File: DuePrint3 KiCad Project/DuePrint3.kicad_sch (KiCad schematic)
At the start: 49 parts, among them J1 430452412, J10 436500215, J11 M20-9990245, J12 M20-9990245, J13 EHT-125-01-S-D, J14 EHT-110-01-S-D, J15 EHT-125-01-S-D, J2 PPPC161LFBN-RC, J3 PPPC161LFBN-RC, J4 6P2C, J5 6P2C, J6 M20-9990345, J7 436500215, J8 436500815, J9 430451812, U1 SN74AHCT125DR

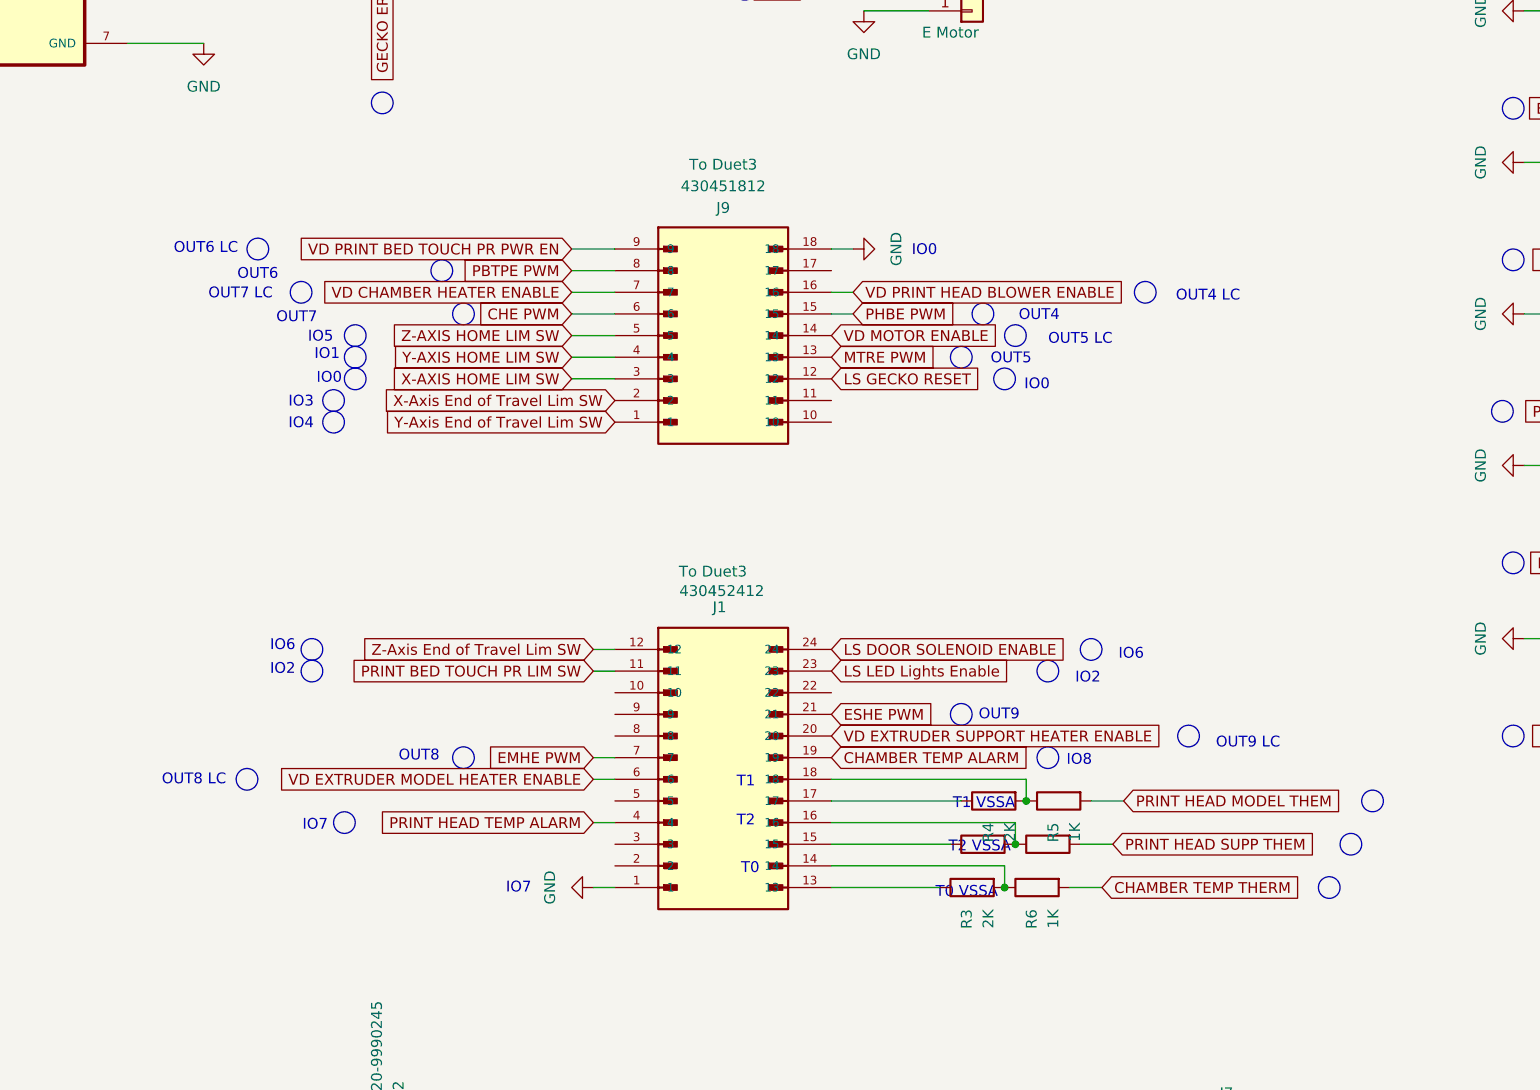
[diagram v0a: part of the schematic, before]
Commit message: Reformat Duet3 connectors
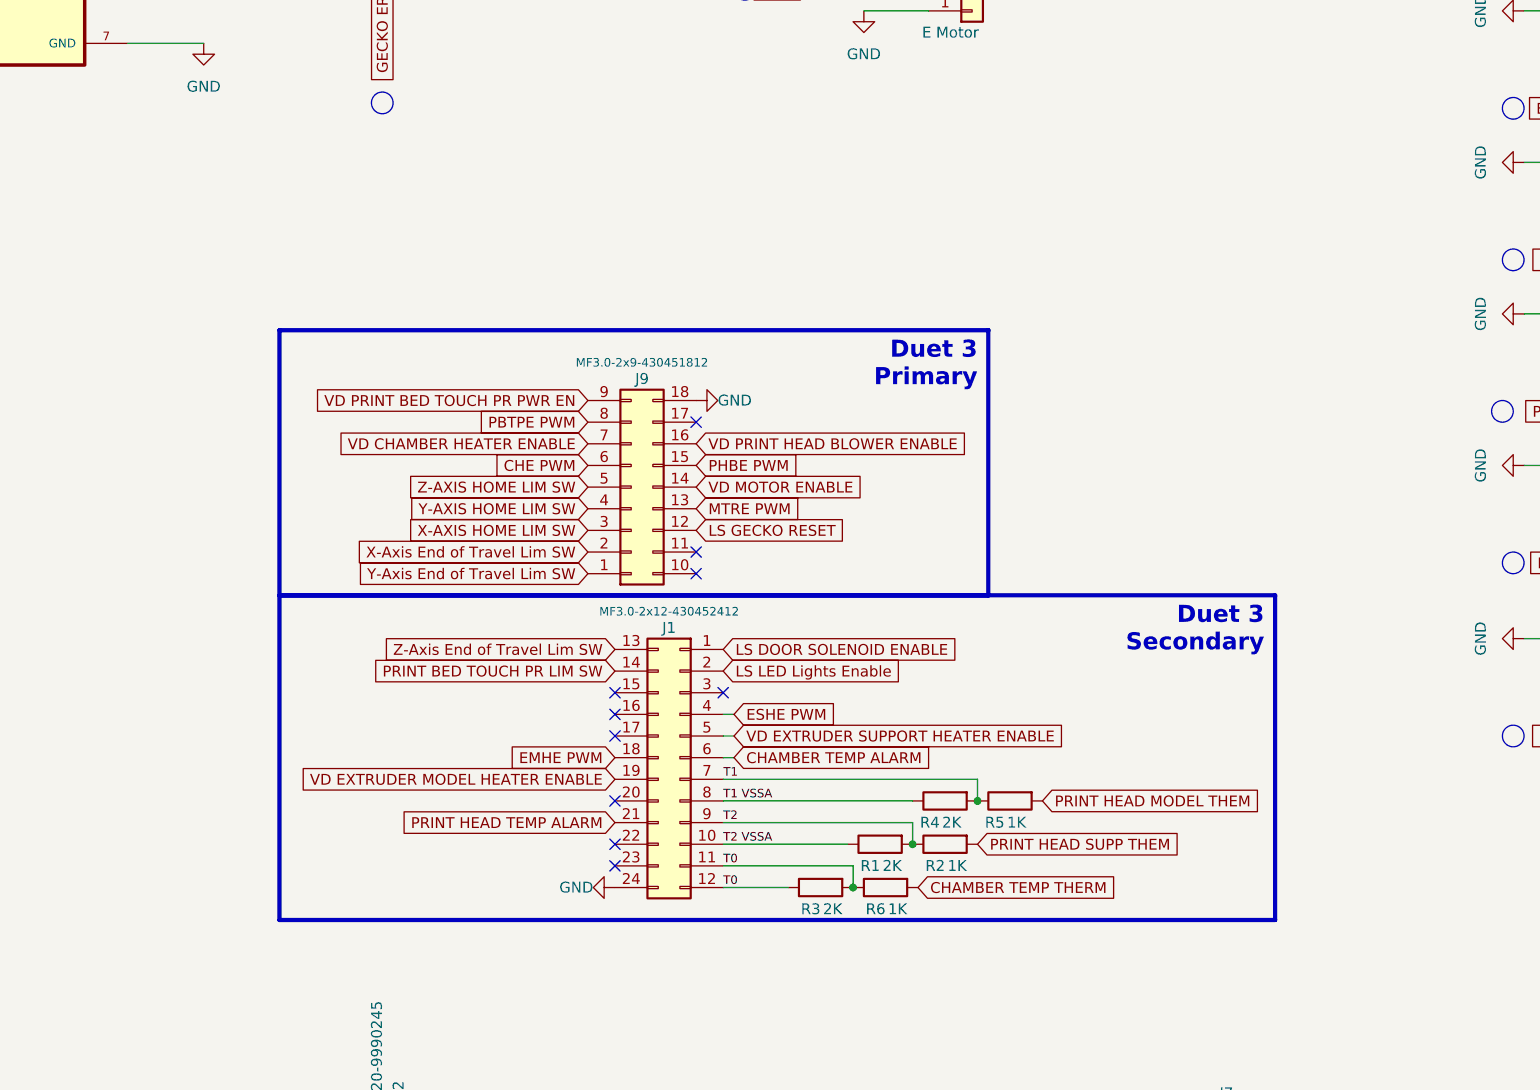
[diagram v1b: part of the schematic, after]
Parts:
- removed J1: 430452412, Connector_Molex:Molex_Micro-Fit_3.0_43045-2412_2x12_P3.00mm_Vertical, symbol 430452427:430452427
- removed J9: 430451812, Connector_Molex:Molex_Micro-Fit_3.0_43045-1812_2x09_P3.00mm_Vertical, symbol Project:430451827
- added J1: MF3.0-2x12-430452412, Connector_Molex:Molex_Micro-Fit_3.0_43045-2412_2x12_P3.00mm_Vertical, symbol Connector_Generic:Conn_02x12_Top_Bottom
- added J9: MF3.0-2x9-430451812, Connector_Molex:Molex_Micro-Fit_3.0_43045-1812_2x09_P3.00mm_Vertical, symbol Connector_Generic:Conn_02x09_Top_Bottom
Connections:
- net CHAMBER HEATER ENABLE: now also J9.6 (Pin_6)
- net CHAMBER TEMP ALARM: now also J1.6 (Pin_6)
- net EMHE PWM: now also J1.18 (Pin_18)
- net ESHE PWM: now also J1.4 (Pin_4)
- net GND: now also J1.24 (Pin_24), J9.18 (Pin_18)
- net LS DOOR SOLENOID ENABLE: now also J1.1 (Pin_1)
- net LS GECKO RESET: now also J9.12 (Pin_12)
- net LS LED Lights Enable: now also J1.2 (Pin_2)
- net MOTOR ENABLE: now also J9.13 (Pin_13)
- net PBTPE PWM: now also J9.8 (Pin_8)
- net PHBE PWM: now also J9.15 (Pin_15)
- net PRINT BED TOUCH PR LIM SW: now also J1.14 (Pin_14)
- net PRINT HEAD TEMP ALARM: now also J1.21 (Pin_21)
- net VD CHAMBER HEATER ENABLE: now also J9.7 (Pin_7)
- net VD EXTRUDER MODEL HEATER ENABLE: now also J1.19 (Pin_19)
- net VD EXTRUDER SUPPORT HEATER ENABLE: now also J1.5 (Pin_5)
- net VD MOTOR ENABLE: now also J9.14 (Pin_14)
- net VD PRINT BED TOUCH PR PWR EN: now also J9.9 (Pin_9)
- net VD PRINT HEAD BLOWER ENABLE: now also J9.16 (Pin_16)
- net X-AXIS HOME LIM SW: now also J9.3 (Pin_3)
- net X-Axis End of Travel Lim SW: now also J9.2 (Pin_2)
- net Y-AXIS HOME LIM SW: now also J9.4 (Pin_4)
- net Y-Axis End of Travel Lim SW: now also J9.1 (Pin_1)
- net Z-AXIS HOME LIM SW: now also J9.5 (Pin_5)
- net Z-Axis End of Travel Lim SW: now also J1.13 (Pin_13)
- net T1 VSSA: now reaches R4.1
- net T1 VSSA: now also J1.8 (Pin_8)
- net T1: now reaches R4.2, R5.1
- net T1: now also J1.7 (Pin_7)
- net T0: now reaches R3.1
- net T0: now also R3.2, R6.1, J1.11 (Pin_11), J1.12 (Pin_12)
- net T2: now reaches R1.2, R2.1
- net T2: now also J1.9 (Pin_9)
- net T2 VSSA: now reaches R1.1
- net T2 VSSA: now also J1.10 (Pin_10)
- no-connect marks 0 -> 10
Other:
- note added: "Duet 3 Primary"
- note added: "Duet 3 Secondary"
- note removed: "IO0"
- note removed: "IO1"
- note removed: "IO2"
- note removed: "IO3"
- note removed: "IO4"
- note removed: "IO5"
- note removed: "IO6"
- note removed: "IO7"
- note removed: "IO8"
- note removed: "OUT4"
- note removed: "OUT4 LC"
- note removed: "OUT5"
- note removed: "OUT5 LC"
- note removed: "OUT6"
- note removed: "OUT6 LC"
- note removed: "OUT7"
- note removed: "OUT7 LC"
- note removed: "OUT8"
- note removed: "OUT8 LC"
- note removed: "OUT9"
- note removed: "OUT9 LC"
- note removed: "T0"
- note removed: "T0 VSSA"
- note removed: "T1"
- note removed: "T1 VSSA"
- note removed: "T2"
- note removed: "T2 VSSA"
- moved on the sheet: R3, R4, R5, R6

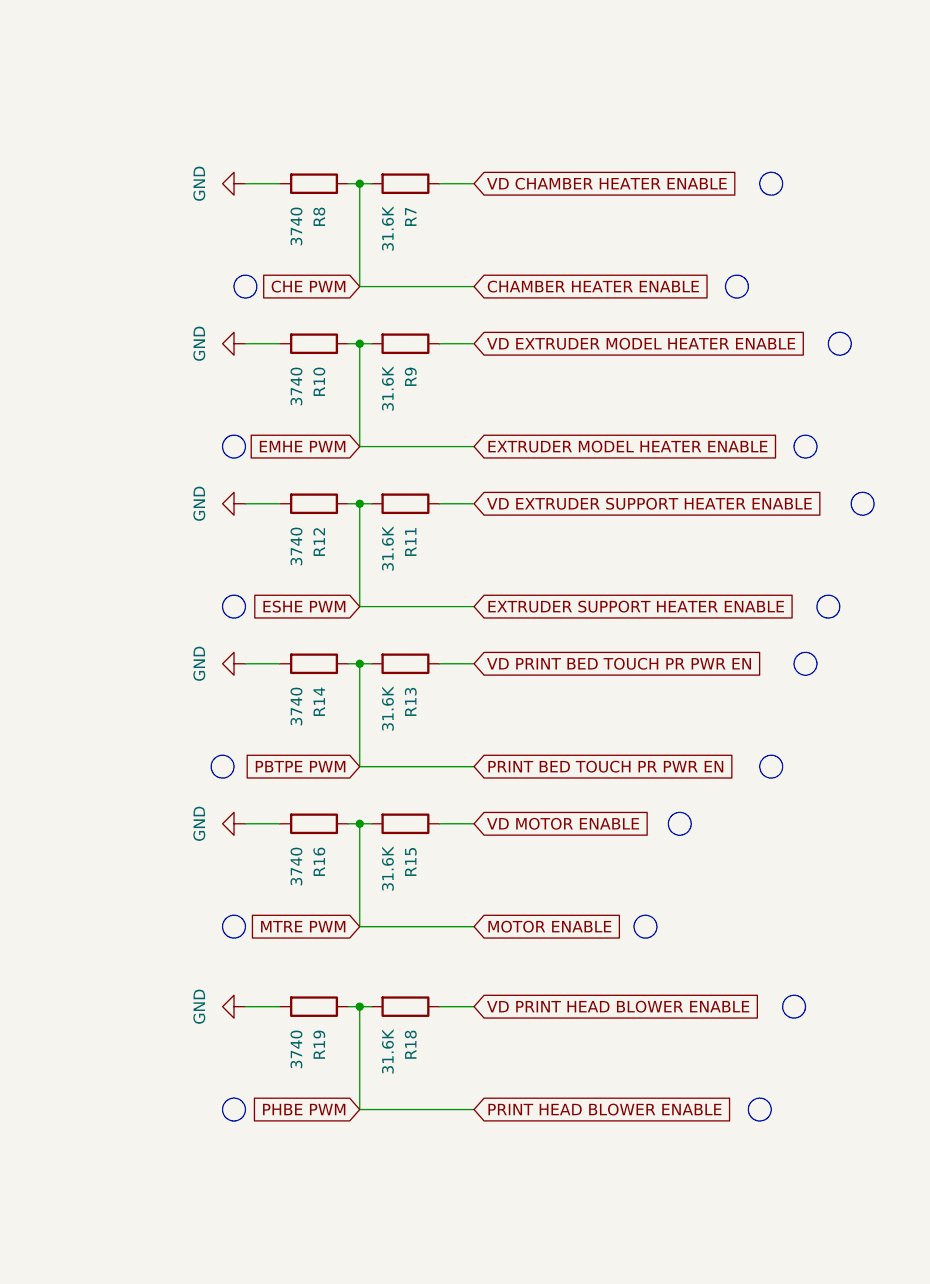
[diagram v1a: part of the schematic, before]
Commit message: Voltage Dividers
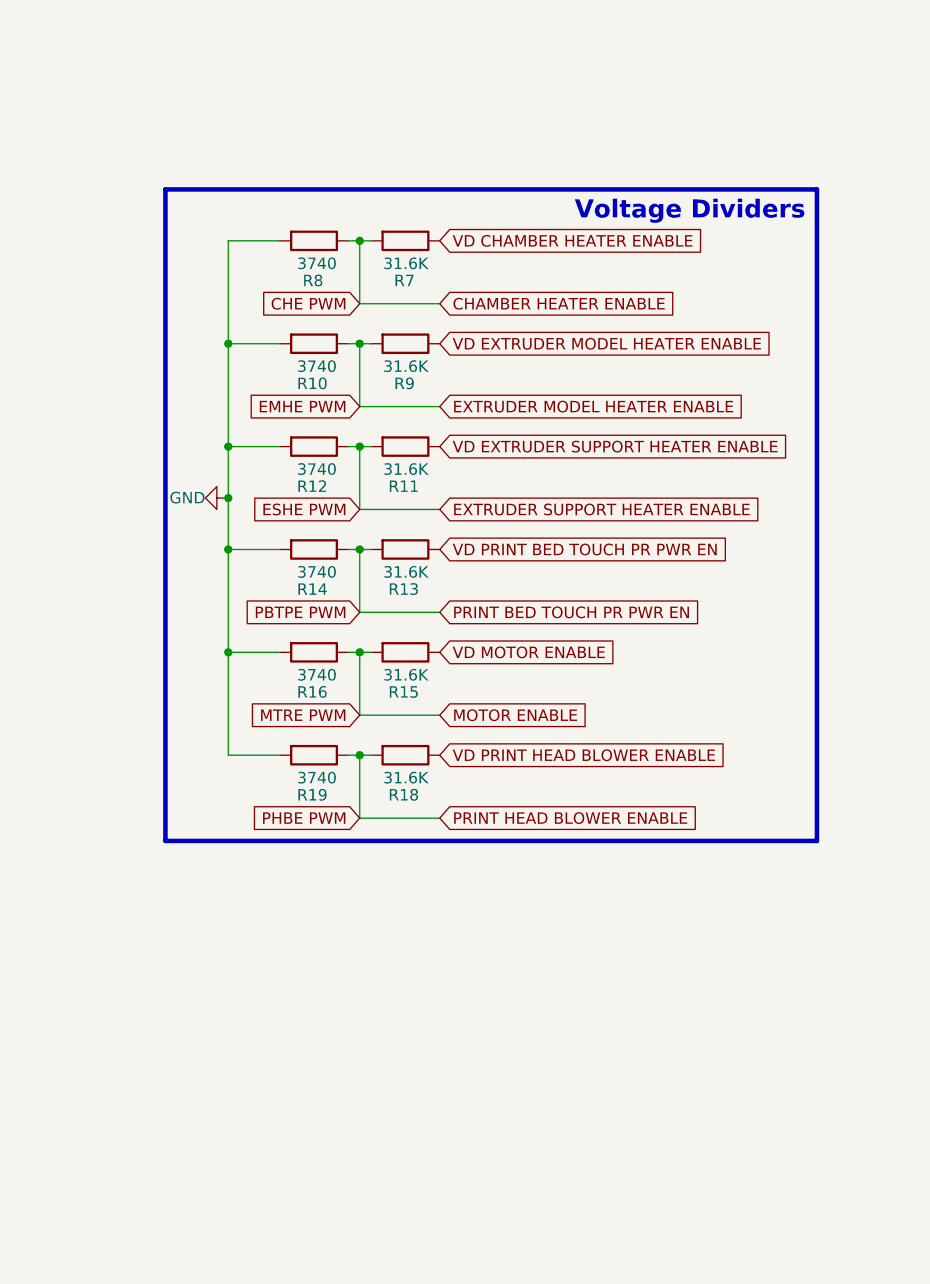
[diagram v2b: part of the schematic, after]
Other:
- note added: "Voltage Dividers"
- moved on the sheet: R11, R12, R13, R14, R15, R16, R18, R19, R7, R8

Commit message: Level shifter
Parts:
- D1: value 100v 1a -> 100v 1A
- J8: value 436500815 -> MF3.0-1x8-436500815; Device E Motor -> (none)
- U1: footprint Stratasys Adapter:SOIC127P600X175-14N -> PCM_Package_SO_AKL:SOIC-14_3.9x8.7mm_P1.27mm
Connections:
- no-connect marks 10 -> 11
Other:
- note added: "Extruder Motor"
- note added: "Level Shifter"
- moved on the sheet: C1, D1, J8

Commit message: PDB Connectors
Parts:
- removed J13, J15: EHT-125-01-S-D, EHT-125-01-S-D:SAMTEC_EHT-125-01-S-D, symbol EHT-125-01-S-D:EHT-125-01-S-D
- removed J14: EHT-110-01-S-D, EHT-110-01-XX-D:EHT-110-01-XX-D, symbol EHT-110-01-XX-D:EHT-110-01-XX-D
- added J13, J15: EHT-125-01-S-D, EHT-125-01-S-D:SAMTEC_EHT-125-01-S-D, symbol Connector_Generic:Conn_02x25_Odd_Even
- added J14: EHT-110-01-S-D, EHT-110-01-XX-D:EHT-110-01-XX-D, symbol Connector_Generic:Conn_02x10_Odd_Even
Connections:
- net +12V: now also J13.49 (Pin_49), J13.50 (Pin_50), J14.19 (Pin_19), J15.49 (Pin_49), J15.50 (Pin_50)
- net +5V: now also J13.47 (Pin_47), J13.48 (Pin_48), J14.17 (Pin_17), J15.16 (Pin_16), J15.47 (Pin_47), J15.48 (Pin_48)
- net ARMATURE NEGATIVE: now also J13.33 (Pin_33)
- net ARMATURE POSITIVE: now also J13.35 (Pin_35)
- net CHAMBER HEATER ENABLE: now also J15.11 (Pin_11)
- net CHAMBER TEMP ALARM: now also J15.33 (Pin_33)
- net CHAMBER TEMP THERM: now also J15.39 (Pin_39)
- net DOOR SOLENOID ENABLE: now also J15.13 (Pin_13)
- net DOOR SWITCH: now also J15.14 (Pin_14)
- net EMHE PWM: now also J15.18 (Pin_18)
- net ENCODER CH A: now also J13.29 (Pin_29)
- net ENCODER CH B: now also J13.31 (Pin_31)
- net ESHE PWM: now also J15.19 (Pin_19)
- net FD1: now also J14.2 (Pin_2)
- net FD2: now also J14.3 (Pin_3)
- net GND: now also J13.10 (Pin_10), J13.13 (Pin_13), J13.14 (Pin_14), J13.16 (Pin_16), J13.18 (Pin_18), J13.2 (Pin_2), J13.20 (Pin_20), J13.22 (Pin_22), J13.24 (Pin_24), J13.26 (Pin_26), J13.28 (Pin_28), J13.30 (Pin_30), J13.32 (Pin_32), J13.34 (Pin_34), J13.36 (Pin_36), J13.38 (Pin_38), J13.4 (Pin_4), J13.40 (Pin_40), J13.42 (Pin_42), J13.44 (Pin_44), J13.46 (Pin_46), J13.8 (Pin_8), J14.1 (Pin_1), J14.13 (Pin_13), J14.15 (Pin_15), J14.16 (Pin_16), J14.18 (Pin_18), J14.20 (Pin_20), J14.5 (Pin_5), J14.9 (Pin_9), J15.1 (Pin_1), J15.17 (Pin_17), J15.20 (Pin_20), J15.24 (Pin_24), J15.26 (Pin_26), J15.28 (Pin_28), J15.34 (Pin_34), J15.36 (Pin_36), J15.38 (Pin_38), J15.40 (Pin_40), J15.45 (Pin_45), J15.46 (Pin_46), J15.9 (Pin_9)
- net HEAD THERMOSTAT STATUS: now also J15.22 (Pin_22)
- net LED Lights Enable: now also J15.12 (Pin_12)
- net MOTOR ENABLE: now also J13.45 (Pin_45)
- net PBTPE PWM: now also J15.15 (Pin_15)
- net PHBE PWM: now also J14.4 (Pin_4)
- net PRINT BED TOUCH PR LIM SW: now also J15.8 (Pin_8)
- net PRINT HEAD MODEL THEM: now also J15.35 (Pin_35)
- net PRINT HEAD SUPP THEM: now also J15.37 (Pin_37)
- net PRINT HEAD TEMP ALARM: now also J15.32 (Pin_32)
- net Print Head Model Toggle SW: now also J14.8 (Pin_8)
- net Print Head Support Toggle SW: now also J14.10 (Pin_10)
- net X-AXIS HOME LIM SW: now also J15.3 (Pin_3)
- net X-Axis End of Travel Lim SW: now also J15.2 (Pin_2)
- net Y-AXIS HOME LIM SW: now also J15.5 (Pin_5)
- net Y-Axis End of Travel Lim SW: now also J15.4 (Pin_4)
- net Z-AXIS HOME LIM SW: now also J15.7 (Pin_7)
- net Z-Axis End of Travel Lim SW: now also J15.6 (Pin_6)
- no-connect marks 11 -> 47
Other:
- note added: "Stratasys PDB - Low"
- note added: "Stratasys PDB - Mid"
- note added: "Stratasys PDB - Top"
- note removed: "J14"
- note removed: "J17"
- note removed: "J18"

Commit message: The Rest Of The Schematic
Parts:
- removed J10, J7: 436500215, Connector_Molex:Molex_Micro-Fit_3.0_43650-0215_1x02_P3.00mm_Vertical, symbol Connector:Conn_01x02_Pin
- removed J11, J12: M20-9990245, Connector_PinHeader_2.54mm:PinHeader_1x02_P2.54mm_Vertical, symbol Connector:Conn_01x02_Pin
- removed J2, J3: PPPC161LFBN-RC, Connector_PinSocket_2.54mm:PinSocket_1x16_P2.54mm_Vertical, symbol Connector:Conn_01x16_Socket
- removed J6: M20-9990345, Connector_PinHeader_2.54mm:PinHeader_1x03_P2.54mm_Vertical, symbol Connector:Conn_01x03_Pin
- added J10, J7: MF3.0-1x2-436500215, Connector_Molex:Molex_Micro-Fit_3.0_43650-0215_1x02_P3.00mm_Vertical, symbol Connector_Generic:Conn_01x02
- added J11, J12: 2.54Header-1x2-M, Connector_PinHeader_2.54mm:PinHeader_1x02_P2.54mm_Vertical, symbol Connector_Generic:Conn_01x02
- added J2, J3: 2.54Header-1x16-F, symbol Connector_Generic:Conn_01x16
- added J6: 2.54Header-1x3-M, symbol Connector_Generic:Conn_01x03
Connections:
- net +12V: now also J10.2 (Pin_2)
- net +5V: now also R24.2, J2.15 (Pin_15), J3.16 (Pin_16), J7.2 (Pin_2); no longer R24.1
- net CAN0H: now also J3.1 (Pin_1), J6.3 (Pin_3)
- net CAN0L: now also J3.2 (Pin_2), J6.1 (Pin_1)
- net DIR: now also J2.11 (Pin_11)
- net DOOR SWITCH: now also J2.7 (Pin_7)
- net FD1: now also J11.1 (Pin_1)
- net FD2: now also J12.1 (Pin_1)
- net GECKO ERROR: now also J2.5 (Pin_5)
- net GND: now also J10.1 (Pin_1), J2.16 (Pin_16), J7.1 (Pin_1)
- net HEAD THERMOSTAT STATUS: now also J2.6 (Pin_6)
- net Print Head Model Toggle SW: now also J3.8 (Pin_8)
- net Print Head Support Toggle SW: now also J2.8 (Pin_8)
- net STEP: now also J2.12 (Pin_12)
- net at R17.2: now also J6.2 (Pin_2)
- net at R25.2: now also J12.2 (Pin_2), J2.3 (Pin_3)
- new net: J11.2 (Pin_2), J2.13 (Pin_13), R24.1
- no-connect marks 47 -> 75
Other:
- note added: "4mm Holes"
- note added: "CAN-FD RJ11 Ports"
- note added: "Power Access"
- note added: "STM32 Extruder"
- note added: "Sammy C21 MCU Module"
- note removed: "Extruder Motor"
- moved on the sheet: C1, D1, H1, H2, H3, H4, H5, H6, J1, J14, J15, J4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
